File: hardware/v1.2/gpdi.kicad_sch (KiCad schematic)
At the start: 20 parts, among them J2 HDMI_C_1.3, U1 ECP5-CABGA256, U5 PCA9306DC1

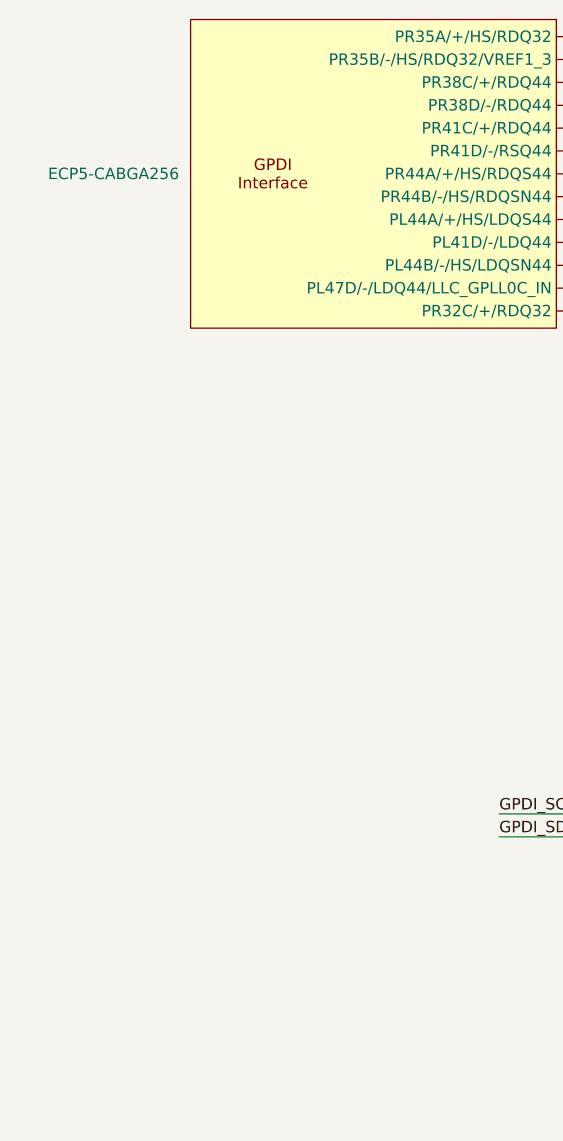
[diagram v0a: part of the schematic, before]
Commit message: UART to PS2 converter
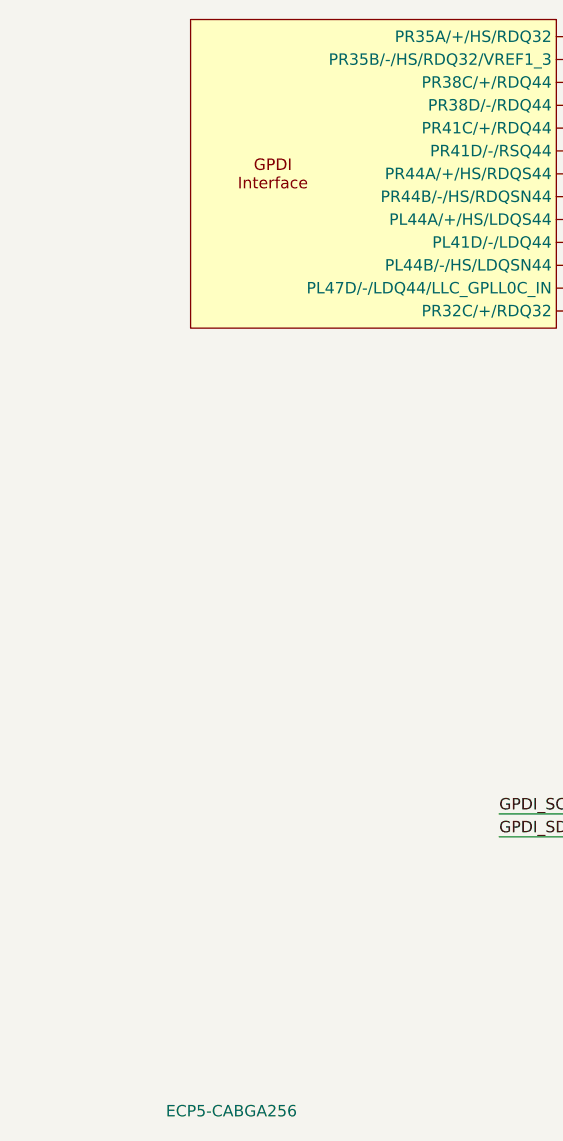
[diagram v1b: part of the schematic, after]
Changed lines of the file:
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@@
 		)
 		(property "Value" "ECP5-CABGA256"
-			(at 64.77 76.2 0)
+			(at 77.8667 180.34 0)
 			(effects
 				(font
@@
 		)
 		(instances
-			(project "icepi-zero"
+			(project ""
+				(path "/f88da08e-cf42-4d03-a08f-3f602fe6658d/17c9c9b3-f379-4e1f-a876-d3fcf0529a4d"
+					(reference "U1")
+					(unit 4)
+				)
 				(path "/f88da08e-cf42-4d03-a08f-3f602fe6658d/efe0a411-ae63-4682-aa63-a9a30697cd67"
 					(reference "U1")
